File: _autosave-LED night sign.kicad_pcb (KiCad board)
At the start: 2 copper layers, 42.9 x 36.7 mm, 24 parts, among them Q1 MOSFET-NCH-2N7002PW, U1 ATtiny85-20P, U2 ATtiny85-20S

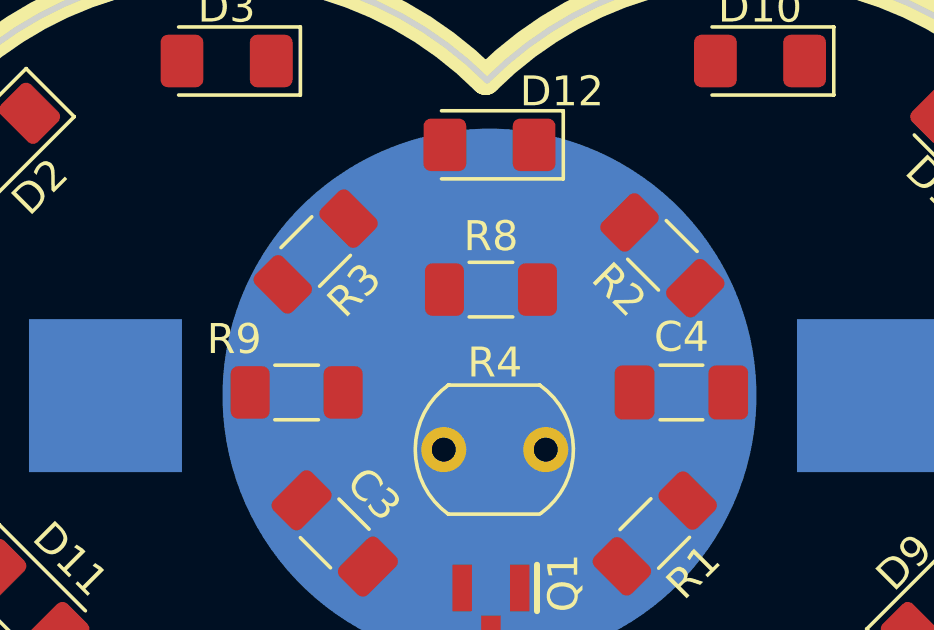
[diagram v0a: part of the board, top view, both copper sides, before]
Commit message: component placement done and starting wiring
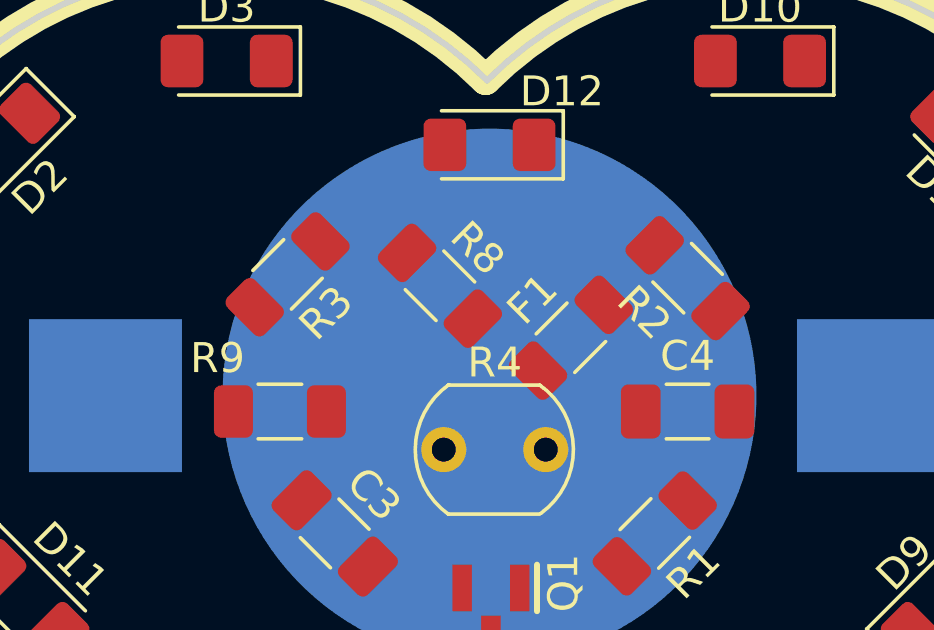
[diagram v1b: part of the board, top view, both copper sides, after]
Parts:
- added F1: Fuse, Resistor_SMD:R_1206_3216Metric_Pad1.30x1.75mm_HandSolder, F.Cu at (152.7, 98.1)
- moved R8 1.70 mm to (148.3, 96.4), turned to 135 degrees
- moved R3 1.21 mm to (143.3, 96.0)
- moved R2 1.13 mm to (156.6, 96.1)
- moved R9 0.84 mm to (143.0, 100.6)
- moved C4 0.67 mm to (156.6, 100.6)
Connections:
- BT1 pad 1: +3V0 -> Net-(BT1-Pad1)
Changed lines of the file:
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@@
   (net 9 "INTL")
   (net 10 "unconnected-(U1-Pad2)")
+  (net 11 "Net-(BT1-Pad1)")
   (footprint "Resistor_SMD:R_1206_3216Metric_Pad1.30x1.75mm_HandSolder" (layer "F.Cu")
-    (at 150.036 96.52 180)
+    (at 148.336 96.393 135)
     (descr "Resistor SMD 1206 (3216 Metric), square (rectangular) end terminal, IPC_7351 nominal with elongated pad for handsoldering. (Body size source: IPC-SM-782 page 72, https://www.pcb-3d.com/wordpress/wp-content/uploads/ipc-sm-782a_amendment_1_and_2.pdf), generated with kicad-footprint-generator")
     (tags "resistor handsolder")
@@
     (property "Sheetname" "")
     (attr smd)
-    (fp_text reference "R8" (at 0 1.778) (layer "F.SilkS")
-      (effects (font (size 1 1) (thickness 0.15)))
-    )
-    (fp_text value "1k" (at 0 1.82) (layer "F.Fab")
-      (effects (font (size 1 1) (thickness 0.15)))
-    )
-    (fp_text user "${REFERENCE}" (at 0 0) (layer "F.Fab")
+    (fp_text reference "R8" (at 0 1.778 135) (layer "F.SilkS")
+      (effects (font (size 1 1) (thickness 0.15)))
+    )
+    (fp_text value "1k" (at 0 1.82 135) (layer "F.Fab")
+      (effects (font (size 1 1) (thickness 0.15)))
+    )
+    (fp_text user "${REFERENCE}" (at 0 0 135) (layer "F.Fab")
       (effects (font (size 0.8 0.8) (thickness 0.12)))
     )
@@
     (fp_line (start -1.6 -0.8) (end 1.6 -0.8) (layer "F.Fab") (width 0.1))
     (fp_line (start 1.6 0.8) (end -1.6 0.8) (layer "F.Fab") (width 0.1))
-    (pad "1" smd roundrect (at -1.55 0 180) (size 1.3 1.75) (layers "F.Cu" "F.Paste" "F.Mask") (roundrect_rratio 0.1923076923)
+    (pad "1" smd roundrect (at -1.55 0 135) (size 1.3 1.75) (layers "F.Cu" "F.Paste" "F.Mask") (roundrect_rratio 0.1923076923)
       (net 4 "Net-(Q1-Pad1)") (pintype "passive"))
-    (pad "2" smd roundrect (at 1.55 0 180) (size 1.3 1.75) (layers "F.Cu" "F.Paste" "F.Mask") (roundrect_rratio 0.1923076923)
+    (pad "2" smd roundrect (at 1.55 0 135) (size 1.3 1.75) (layers "F.Cu" "F.Paste" "F.Mask") (roundrect_rratio 0.1923076923)
       (net 7 "CTRLLED") (pintype "passive"))
     (model "${KIPRJMOD}/packages3D/R_1206_3216Metric.wrl"
@@
   )
   (footprint "Resistor_SMD:R_1206_3216Metric_Pad1.30x1.75mm_HandSolder" (layer "F.Cu")
-    (at 143.559 99.949)
+    (at 143.002 100.584)
     (descr "Resistor SMD 1206 (3216 Metric), square (rectangular) end terminal, IPC_7351 nominal with elongated pad for handsoldering. (Body size source: IPC-SM-782 page 72, https://www.pcb-3d.com/wordpress/wp-content/uploads/ipc-sm-782a_amendment_1_and_2.pdf), generated with kicad-footprint-generator")
     (tags "resistor handsolder")
@@
   )
   (footprint "Resistor_SMD:R_1206_3216Metric_Pad1.30x1.75mm_HandSolder" (layer "F.Cu")
-    (at 144.194 95.25 -135)
+    (at 143.256 96.012 -135)
     (descr "Resistor SMD 1206 (3216 Metric), square (rectangular) end terminal, IPC_7351 nominal with elongated pad for handsoldering. (Body size source: IPC-SM-782 page 72, https://www.pcb-3d.com/wordpress/wp-content/uploads/ipc-sm-782a_amendment_1_and_2.pdf), generated with kicad-footprint-generator")
     (tags "resistor handsolder")
@@
   )
   (footprint "Resistor_SMD:R_1206_3216Metric_Pad1.30x1.75mm_HandSolder" (layer "F.Cu")
-    (at 155.751 95.377 -45)
+    (at 156.591 96.139 -45)
     (descr "Resistor SMD 1206 (3216 Metric), square (rectangular) end terminal, IPC_7351 nominal with elongated pad for handsoldering. (Body size source: IPC-SM-782 page 72, https://www.pcb-3d.com/wordpress/wp-content/uploads/ipc-sm-782a_amendment_1_and_2.pdf), generated with kicad-footprint-generator")
     (tags "resistor handsolder")
@@
   )
   (footprint "Capacitor_SMD:C_1206_3216Metric_Pad1.33x1.80mm_HandSolder" (layer "F.Cu")
-    (at 156.386 99.949)
+    (at 156.591 100.584)
     (descr "Capacitor SMD 1206 (3216 Metric), square (rectangular) end terminal, IPC_7351 nominal with elongated pad for handsoldering. (Body size source: IPC-SM-782 page 76, https://www.pcb-3d.com/wordpress/wp-content/uploads/ipc-sm-782a_amendment_1_and_2.pdf), generated with kicad-footprint-generator")
     (tags "capacitor handsolder")
@@
       (net 2 "+3V0") (pinfunction "A") (pintype "passive"))
     (model "${KIPRJMOD}/packages3D/LED_1206_3216Metric.wrl"
+      (offset (xyz 0 0 0))
+      (scale (xyz 1 1 1))
+      (rotate (xyz 0 0 0))
+    )
+  )
+  (footprint "Resistor_SMD:R_1206_3216Metric_Pad1.30x1.75mm_HandSolder" (layer "F.Cu")
+    (at 152.700984 98.124016 45)
+    (descr "Resistor SMD 1206 (3216 Metric), square (rectangular) end terminal, IPC_7351 nominal with elongated pad for handsoldering. (Body size source: IPC-SM-782 page 72, https://www.pcb-3d.com/wordpress/wp-content/uploads/ipc-sm-782a_amendment_1_and_2.pdf), generated with kicad-footprint-generator")
+    (tags "resistor handsolder")
+    (property "Sheetfile" "LED night sign.kicad_sch")
+    (property "Sheetname" "")
+    (attr smd)
+    (fp_text reference "F1" (at 0 -1.82 45) (layer "F.SilkS")
+      (effects (font (size 1 1) (thickness 0.15)))
+    )
+    (fp_text value "Fuse" (at 0 1.82 45) (layer "F.Fab")
+      (effects (font (size 1 1) (thickness 0.15)))
+    )
+    (fp_text user "${REFERENCE}" (at 0 0 45) (layer "F.Fab")
+      (effects (font (size 0.8 0.8) (thickness 0.12)))
+    )
+    (fp_line (start -0.727064 -0.91) (end 0.727064 -0.91) (layer "F.SilkS") (width 0.12))
+    (fp_line (start -0.727064 0.91) (end 0.727064 0.91) (layer "F.SilkS") (width 0.12))
+    (fp_line (start 2.45 -1.12) (end 2.45 1.12) (layer "F.CrtYd") (width 0.05))
+    (fp_line (start -2.45 1.12) (end -2.45 -1.12) (layer "F.CrtYd") (width 0.05))
+    (fp_line (start 2.45 1.12) (end -2.45 1.12) (layer "F.CrtYd") (width 0.05))
+    (fp_line (start -2.45 -1.12) (end 2.45 -1.12) (layer "F.CrtYd") (width 0.05))
+    (fp_line (start -1.6 -0.8) (end 1.6 -0.8) (layer "F.Fab") (width 0.1))
+    (fp_line (start 1.6 -0.8) (end 1.6 0.8) (layer "F.Fab") (width 0.1))
+    (fp_line (start -1.6 0.8) (end -1.6 -0.8) (layer "F.Fab") (width 0.1))
+    (fp_line (start 1.6 0.8) (end -1.6 0.8) (layer "F.Fab") (width 0.1))
+    (pad "1" smd roundrect (at -1.55 0 45) (size 1.3 1.75) (layers "F.Cu" "F.Paste" "F.Mask") (roundrect_rratio 0.192308)
+      (net 2 "+3V0") (pintype "passive"))
+    (pad "2" smd roundrect (at 1.55 0 45) (size 1.3 1.75) (layers "F.Cu" "F.Paste" "F.Mask") (roundrect_rratio 0.192308)
+      (net 11 "Net-(BT1-Pad1)") (pintype "passive"))
+    (model "${KICAD6_3DMODEL_DIR}/Resistor_SMD.3dshapes/R_1206_3216Metric.wrl"
       (offset (xyz 0 0 0))
       (scale (xyz 1 1 1))
@@
     (fp_line (start -15.35 -2.55) (end -10.55 -2.55) (layer "B.Fab") (width 0.1))
     (pad "1" smd rect (at -12.8 0 180) (size 5.1 5.1) (layers "B.Cu" "B.Paste" "B.Mask")
-      (net 2 "+3V0") (pinfunction "+") (pintype "passive"))
+      (net 11 "Net-(BT1-Pad1)") (pinfunction "+") (pintype "passive"))
     (pad "1" smd rect (at 12.8 0 180) (size 5.1 5.1) (layers "B.Cu" "B.Paste" "B.Mask")
-      (net 2 "+3V0") (pinfunction "+") (pintype "passive"))
+      (net 11 "Net-(BT1-Pad1)") (pinfunction "+") (pintype "passive"))
     (pad "2" smd circle (at 0 0 180) (size 17.8 17.8) (layers "B.Cu" "B.Mask")
       (net 1 "GND") (pinfunction "-") (pintype "passive"))
